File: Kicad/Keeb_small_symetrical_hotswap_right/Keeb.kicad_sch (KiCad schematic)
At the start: 20 parts, among them J1 TYPE-C-31-M-12, SW1 CherryMX, SW10 CherryMX, SW11 CherryMX, SW13 CherryMX, SW14 CherryMX, SW15 CherryMX, SW16 CherryMX, SW17 CherryMX, SW18 CherryMX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

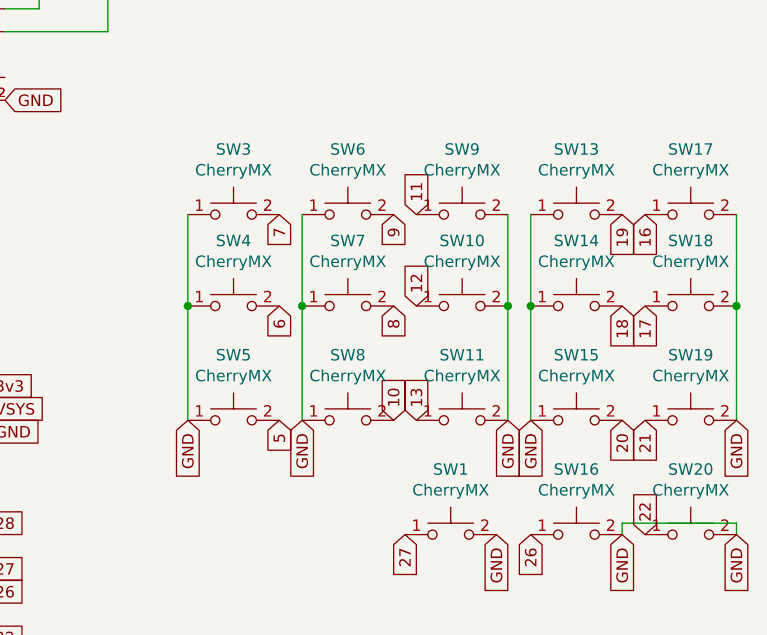
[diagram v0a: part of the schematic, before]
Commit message: Started work on the right half, fixed routing in the left half
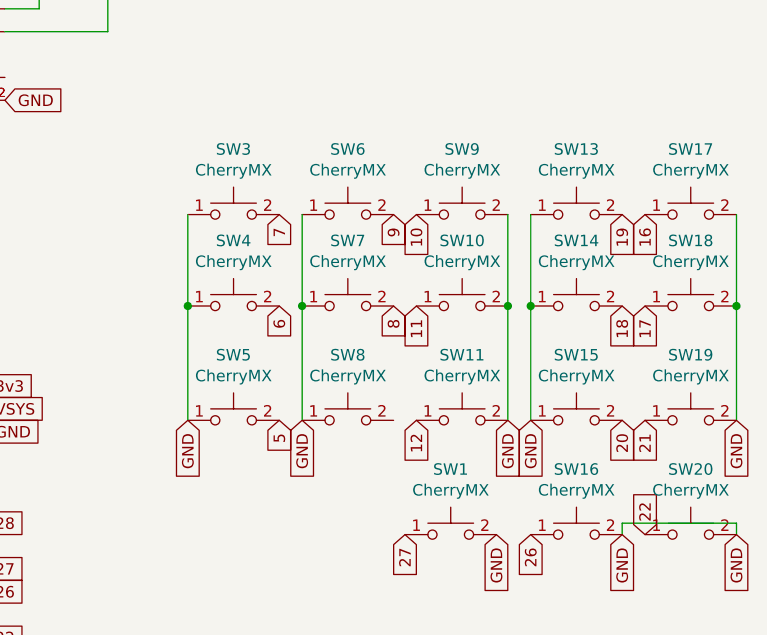
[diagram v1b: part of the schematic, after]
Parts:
- J1: footprint USB-C-Power-tester:TYPE-C-31-M-12 -> TypeC:HRO_TYPE-C-31-M-12
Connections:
- net 10: now also SW9.1; no longer SW8.2
- net 11: now also SW10.1; no longer SW9.1
- net 12: now also SW11.1; no longer SW10.1
- net 13: no longer SW11.1
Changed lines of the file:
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@@
+    )
+  )
+  (global_label "11" (shape input) (at 133.35 72.39 270) (fields_autoplaced)
+    (effects (font (size 1.27 1.27)) (justify right))
+    (property "Intersheetrefs" "${INTERSHEET_REFS}" (at 133.35 77.14 90)
+      (effects (font (size 1.27 1.27)) (justify right) hide)
     )
   )
@@
     )
   )
-  (global_label "11" (shape input) (at 133.35 62.23 90) (fields_autoplaced)
-    (effects (font (size 1.27 1.27)) (justify left))
-    (property "Intersheetrefs" "${INTERSHEET_REFS}" (at 133.35 57.48 90)
-      (effects (font (size 1.27 1.27)) (justify left) hide)
-    )
-  )
   (global_label "4" (shape input) (at 49.53 93.98 180) (fields_autoplaced)
     (effects (font (size 1.27 1.27)) (justify right))
@@
     )
   )
-  (global_label "10" (shape input) (at 130.81 85.09 90) (fields_autoplaced)
-    (effects (font (size 1.27 1.27)) (justify left))
-    (property "Intersheetrefs" "${INTERSHEET_REFS}" (at 130.81 80.34 90)
-      (effects (font (size 1.27 1.27)) (justify left) hide)
-    )
-  )
   (global_label "GND" (shape input) (at 85.09 111.76 0) (fields_autoplaced)
     (effects (font (size 1.27 1.27)) (justify left))
@@
     )
   )
-  (global_label "12" (shape input) (at 133.35 72.39 90) (fields_autoplaced)
-    (effects (font (size 1.27 1.27)) (justify left))
-    (property "Intersheetrefs" "${INTERSHEET_REFS}" (at 133.35 67.64 90)
-      (effects (font (size 1.27 1.27)) (justify left) hide)
-    )
-  )
   (global_label "0" (shape input) (at 49.53 81.28 180) (fields_autoplaced)
     (effects (font (size 1.27 1.27)) (justify right))
@@
     )
   )
+  (global_label "12" (shape input) (at 133.35 85.09 270) (fields_autoplaced)
+    (effects (font (size 1.27 1.27)) (justify right))
+    (property "Intersheetrefs" "${INTERSHEET_REFS}" (at 133.35 89.84 90)
+      (effects (font (size 1.27 1.27)) (justify right) hide)
+    )
+  )
   (global_label "12" (shape input) (at 49.53 119.38 180) (fields_autoplaced)
     (effects (font (size 1.27 1.27)) (justify right))
@@
     )
   )
-  (global_label "13" (shape input) (at 133.35 85.09 90) (fields_autoplaced)
-    (effects (font (size 1.27 1.27)) (justify left))
-    (property "Intersheetrefs" "${INTERSHEET_REFS}" (at 133.35 80.34 90)
-      (effects (font (size 1.27 1.27)) (justify left) hide)
-    )
-  )
   (global_label "1" (shape input) (at 48.26 36.83 180) (fields_autoplaced)
     (effects (font (size 1.27 1.27)) (justify right))
@@
     (property "Intersheetrefs" "${INTERSHEET_REFS}" (at 92.0172 83.82 0)
       (effects (font (size 1.27 1.27)) (justify left) hide)
+    )
+  )
+  (global_label "10" (shape input) (at 133.35 62.23 270) (fields_autoplaced)
+    (effects (font (size 1.27 1.27)) (justify right))
+    (property "Intersheetrefs" "${INTERSHEET_REFS}" (at 133.35 66.98 90)
+      (effects (font (size 1.27 1.27)) (justify right) hide)
     )
   )
@@
       (effects (font (size 1.27 1.27)))
     )
-    (property "Footprint" "USB-C-Power-tester:TYPE-C-31-M-12" (at 69.85 39.37 0)
+    (property "Footprint" "TypeC:HRO_TYPE-C-31-M-12" (at 69.85 39.37 0)
       (effects (font (size 1.27 1.27)) (justify bottom) hide)
     )

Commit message: MVP of the right half
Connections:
- net 10: no longer SW9.1
- net 11: now also SW15.2; no longer SW10.1
- net 12: now also SW14.2; no longer SW11.1
- net 13: now also SW13.2
- net 16: now also SW11.1; no longer SW17.1
- net 17: now also SW10.1; no longer SW18.1
- net 18: now also SW9.1; no longer SW14.2
- net 19: now also SW8.2; no longer SW13.2
- net 20: now also SW7.2; no longer SW15.2
- net 21: now also SW6.2; no longer SW19.1
- net 22: no longer SW20.1
- net 26: now also SW3.2; no longer SW16.1
- net 27: now also SW4.2; no longer SW1.1
- net 28: now also SW5.2
- net 3v3: now also J1.B5 (CC2), J1.B8 (SBU2); no longer J1.A4_B9 (VBUS), J1.B4_A9 (VBUS)
- net 4: now also SW1.1
- net 5: now also SW16.1; no longer SW5.2
- net 6: now also SW20.1; no longer SW4.2
- net 7: now also SW19.1; no longer SW3.2
- net 8: now also SW18.1; no longer SW7.2
- net 9: now also SW17.1; no longer SW6.2
- net VSYS: now also J1.A4_B9 (VBUS), J1.B4_A9 (VBUS); no longer J1.B5 (CC2), J1.B8 (SBU2)

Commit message: rm holes for controller
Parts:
- U1: footprint MCU_RaspberryPi_and_Boards:RPi_Pico_SMD_TH -> MCU_RaspberryPi_and_Boards:RPi_Pico_SMD_TH_NO_HOLES
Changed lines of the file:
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@@
       (effects (font (size 1.27 1.27)))
     )
-    (property "Footprint" "MCU_RaspberryPi_and_Boards:RPi_Pico_SMD_TH" (at 67.31 105.41 90)
+    (property "Footprint" "MCU_RaspberryPi_and_Boards:RPi_Pico_SMD_TH_NO_HOLES" (at 67.31 105.41 90)
       (effects (font (size 1.27 1.27)) hide)
     )

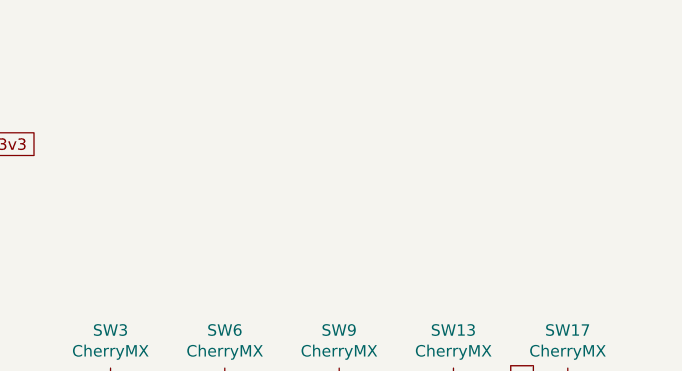
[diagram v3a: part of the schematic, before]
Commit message: Added mounting holes to the PCB
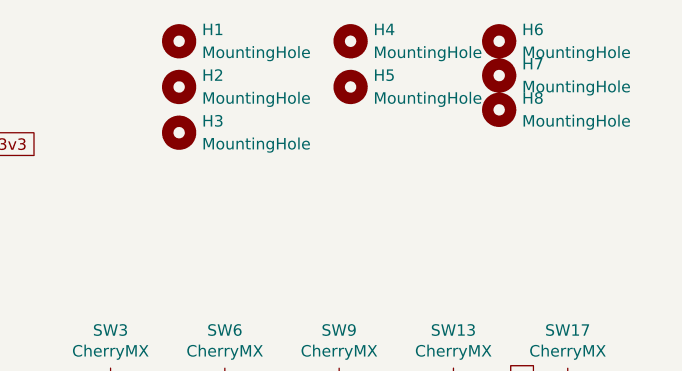
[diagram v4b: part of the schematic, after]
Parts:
- added H1, H2, H3, H4, H5, H6, H7, H8: MountingHole, MountingHole:MountingHole_3.2mm_M3, symbol Mechanical:MountingHole
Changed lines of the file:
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@@
+    )
+  )
+  (symbol (lib_id "Mechanical:MountingHole") (at 156.21 30.48 0) (unit 1)
+    (in_bom yes) (on_board yes) (dnp no) (fields_autoplaced)
+    (property "Reference" "H8" (at 158.75 29.21 0)
+      (effects (font (size 1.27 1.27)) (justify left))
+    )
+    (property "Value" "MountingHole" (at 158.75 31.75 0)
+      (effects (font (size 1.27 1.27)) (justify left))
+    )
+    (property "Footprint" "MountingHole:MountingHole_3.2mm_M3" (at 156.21 30.48 0)
+      (effects (font (size 1.27 1.27)) hide)
+    )
+    (property "Datasheet" "~" (at 156.21 30.48 0)
+      (effects (font (size 1.27 1.27)) hide)
+    )
+    (instances
+      (project "Keeb"
+        (path "/f8892ba2-997e-41dc-a7e4-c2b6962ff100"
+          (reference "H8") (unit 1)
+        )
+      )
+    )
+  )
+  (symbol (lib_id "Mechanical:MountingHole") (at 156.21 26.67 0) (unit 1)
+    (in_bom yes) (on_board yes) (dnp no) (fields_autoplaced)
+    (property "Reference" "H7" (at 158.75 25.4 0)
+      (effects (font (size 1.27 1.27)) (justify left))
+    )
+    (property "Value" "MountingHole" (at 158.75 27.94 0)
+      (effects (font (size 1.27 1.27)) (justify left))
+    )
+    (property "Footprint" "MountingHole:MountingHole_3.2mm_M3" (at 156.21 26.67 0)
+      (effects (font (size 1.27 1.27)) hide)
+    )
+    (property "Datasheet" "~" (at 156.21 26.67 0)
+      (effects (font (size 1.27 1.27)) hide)
+    )
+    (instances
+      (project "Keeb"
+        (path "/f8892ba2-997e-41dc-a7e4-c2b6962ff100"
+          (reference "H7") (unit 1)
+        )
+      )
+    )
+  )
+  (symbol (lib_id "Mechanical:MountingHole") (at 139.7 27.94 0) (unit 1)
+    (in_bom yes) (on_board yes) (dnp no) (fields_autoplaced)
+    (property "Reference" "H5" (at 142.24 26.67 0)
+      (effects (font (size 1.27 1.27)) (justify left))
+    )
+    (property "Value" "MountingHole" (at 142.24 29.21 0)
+      (effects (font (size 1.27 1.27)) (justify left))
+    )
+    (property "Footprint" "MountingHole:MountingHole_3.2mm_M3" (at 139.7 27.94 0)
+      (effects (font (size 1.27 1.27)) hide)
+    )
+    (property "Datasheet" "~" (at 139.7 27.94 0)
+      (effects (font (size 1.27 1.27)) hide)
+    )
+    (instances
+      (project "Keeb"
+        (path "/f8892ba2-997e-41dc-a7e4-c2b6962ff100"
+          (reference "H5") (unit 1)
+        )
+      )
+    )
+  )
+  (symbol (lib_id "Mechanical:MountingHole") (at 156.21 22.86 0) (unit 1)
+    (in_bom yes) (on_board yes) (dnp no) (fields_autoplaced)
+    (property "Reference" "H6" (at 158.75 21.59 0)
+      (effects (font (size 1.27 1.27)) (justify left))
+    )
+    (property "Value" "MountingHole" (at 158.75 24.13 0)
+      (effects (font (size 1.27 1.27)) (justify left))
+    )
+    (property "Footprint" "MountingHole:MountingHole_3.2mm_M3" (at 156.21 22.86 0)
+      (effects (font (size 1.27 1.27)) hide)
+    )
+    (property "Datasheet" "~" (at 156.21 22.86 0)
+      (effects (font (size 1.27 1.27)) hide)
+    )
+    (instances
+      (project "Keeb"
+        (path "/f8892ba2-997e-41dc-a7e4-c2b6962ff100"
+          (reference "H6") (unit 1)
+        )
+      )
+    )
+  )
+  (symbol (lib_id "Mechanical:MountingHole") (at 120.65 33.02 0) (unit 1)
+    (in_bom yes) (on_board yes) (dnp no) (fields_autoplaced)
+    (property "Reference" "H3" (at 123.19 31.75 0)
+      (effects (font (size 1.27 1.27)) (justify left))
+    )
+    (property "Value" "MountingHole" (at 123.19 34.29 0)
+      (effects (font (size 1.27 1.27)) (justify left))
+    )
+    (property "Footprint" "MountingHole:MountingHole_3.2mm_M3" (at 120.65 33.02 0)
+      (effects (font (size 1.27 1.27)) hide)
+    )
+    (property "Datasheet" "~" (at 120.65 33.02 0)
+      (effects (font (size 1.27 1.27)) hide)
+    )
+    (instances
+      (project "Keeb"
+        (path "/f8892ba2-997e-41dc-a7e4-c2b6962ff100"
+          (reference "H3") (unit 1)
+        )
+      )
+    )
+  )
+  (symbol (lib_id "Mechanical:MountingHole") (at 139.7 22.86 0) (unit 1)
+    (in_bom yes) (on_board yes) (dnp no) (fields_autoplaced)
+    (property "Reference" "H4" (at 142.24 21.59 0)
+      (effects (font (size 1.27 1.27)) (justify left))
+    )
+    (property "Value" "MountingHole" (at 142.24 24.13 0)
+      (effects (font (size 1.27 1.27)) (justify left))
+    )
+    (property "Footprint" "MountingHole:MountingHole_3.2mm_M3" (at 139.7 22.86 0)
+      (effects (font (size 1.27 1.27)) hide)
+    )
+    (property "Datasheet" "~" (at 139.7 22.86 0)
+      (effects (font (size 1.27 1.27)) hide)
+    )
+    (instances
+      (project "Keeb"
+        (path "/f8892ba2-997e-41dc-a7e4-c2b6962ff100"
+          (reference "H4") (unit 1)
+        )
+      )
+    )
+  )
+  (symbol (lib_id "Mechanical:MountingHole") (at 120.65 22.86 0) (unit 1)
+    (in_bom yes) (on_board yes) (dnp no) (fields_autoplaced)
+    (property "Reference" "H1" (at 123.19 21.59 0)
+      (effects (font (size 1.27 1.27)) (justify left))
+    )
+    (property "Value" "MountingHole" (at 123.19 24.13 0)
+      (effects (font (size 1.27 1.27)) (justify left))
+    )
+    (property "Footprint" "MountingHole:MountingHole_3.2mm_M3" (at 120.65 22.86 0)
+      (effects (font (size 1.27 1.27)) hide)
+    )
+    (property "Datasheet" "~" (at 120.65 22.86 0)
+      (effects (font (size 1.27 1.27)) hide)
+    )
+    (instances
+      (project "Keeb"
+        (path "/f8892ba2-997e-41dc-a7e4-c2b6962ff100"
+          (reference "H1") (unit 1)
+        )
+      )
+    )
+  )
+  (symbol (lib_id "Mechanical:MountingHole") (at 120.65 27.94 0) (unit 1)
+    (in_bom yes) (on_board yes) (dnp no) (fields_autoplaced)
+    (property "Reference" "H2" (at 123.19 26.67 0)
+      (effects (font (size 1.27 1.27)) (justify left))
+    )
+    (property "Value" "MountingHole" (at 123.19 29.21 0)
+      (effects (font (size 1.27 1.27)) (justify left))
+    )
+    (property "Footprint" "MountingHole:MountingHole_3.2mm_M3" (at 120.65 27.94 0)
+      (effects (font (size 1.27 1.27)) hide)
+    )
+    (property "Datasheet" "~" (at 120.65 27.94 0)
+      (effects (font (size 1.27 1.27)) hide)
+    )
+    (instances
+      (project "Keeb"
+        (path "/f8892ba2-997e-41dc-a7e4-c2b6962ff100"
+          (reference "H2") (unit 1)
+        )
+      )
     )
   )
